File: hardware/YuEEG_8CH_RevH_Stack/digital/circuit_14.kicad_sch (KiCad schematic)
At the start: 6 parts

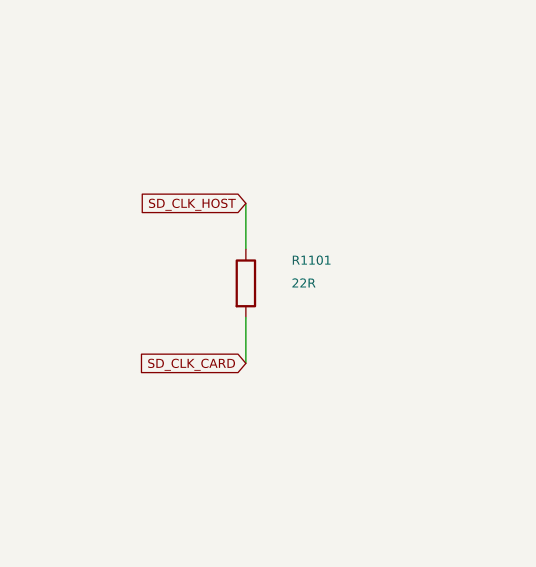
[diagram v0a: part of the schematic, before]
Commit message: Constrain display clearance resistor height and audit remaining design gates
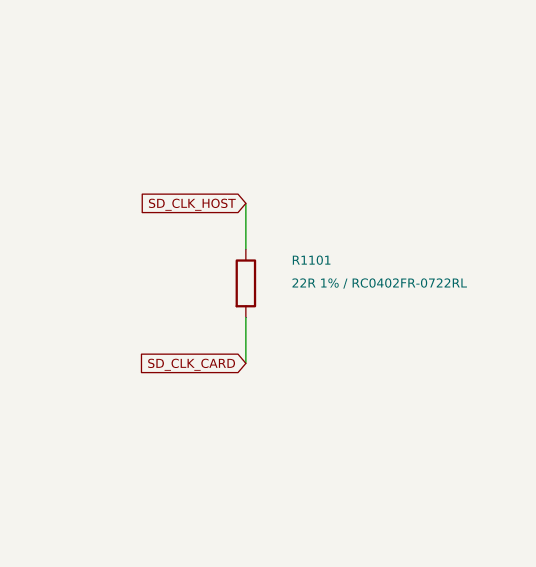
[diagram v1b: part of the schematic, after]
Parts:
- R1101: value 22R -> 22R 1% / RC0402FR-0722RL; footprint Resistor_SMD:R_0402_1005Metric -> YuEEG:YAGEO_RC0402FR_0722RL
